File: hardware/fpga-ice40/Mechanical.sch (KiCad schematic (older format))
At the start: 2 parts

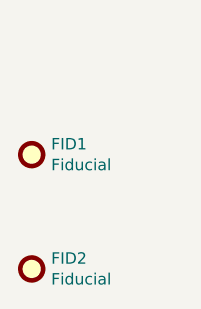
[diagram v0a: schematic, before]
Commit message: Swap in Nelgau-Logo symbol footprint
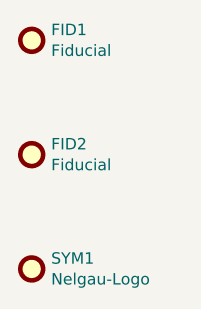
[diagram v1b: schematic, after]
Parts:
- added SYM1: Nelgau-Logo, ng_symbol:Nelgau-Logo_5.2x1.7mm_SilkScreen, symbol ng_symbol:Symbol
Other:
- moved on the sheet: FID1, FID2
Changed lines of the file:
@@
 L Mechanical:Fiducial FID1
 U 1 1 5F487E71
+P 5000 3500
+F 0 "FID1" H 5085 3546 50  0000 L CNN
+F 1 "Fiducial" H 5085 3455 50  0000 L CNN
+F 2 "Fiducial:Fiducial_1mm_Mask2mm" H 5000 3500 50  0001 C CNN
+F 3 "~" H 5000 3500 50  0001 C CNN
+	1    5000 3500
+	1    0    0    -1
+$EndComp
+$Comp
+L Mechanical:Fiducial FID2
+U 1 1 5F488542
 P 5000 4000
-F 0 "FID1" H 5085 4046 50  0000 L CNN
+F 0 "FID2" H 5085 4046 50  0000 L CNN
 F 1 "Fiducial" H 5085 3955 50  0000 L CNN
 F 2 "Fiducial:Fiducial_1mm_Mask2mm" H 5000 4000 50  0001 C CNN
@@
 $EndComp
 $Comp
-L Mechanical:Fiducial FID2
-U 1 1 5F488542
+L ng_symbol:Symbol SYM1
+U 1 1 5F179F68
 P 5000 4500
-F 0 "FID2" H 5085 4546 50  0000 L CNN
-F 1 "Fiducial" H 5085 4455 50  0000 L CNN
-F 2 "Fiducial:Fiducial_1mm_Mask2mm" H 5000 4500 50  0001 C CNN
-F 3 "~" H 5000 4500 50  0001 C CNN
+F 0 "SYM1" H 5085 4546 50  0000 L CNN
+F 1 "Nelgau-Logo" H 5085 4455 50  0000 L CNN
+F 2 "ng_symbol:Nelgau-Logo_5.2x1.7mm_SilkScreen" H 5000 4500 50  0001 C CNN
+F 3 "" H 5000 4500 50  0001 C CNN
 	1    5000 4500
 	1    0    0    -1
